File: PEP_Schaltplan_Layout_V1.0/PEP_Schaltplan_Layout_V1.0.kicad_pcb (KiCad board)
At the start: 2 copper layers, 202.5 x 119.7 mm, 140 parts, among them J1 Conn_01x02_Pin, J10 Conn_01x01_Pin, J11 Conn_01x02_Pin, J12 Conn_01x01_Pin, J2 Conn_01x01_Pin, J3 Conn_01x01_Pin, J4 Conn_01x01_Pin, J5 Conn_01x01_Pin, J6 Conn_01x01_Pin, J7 Conn_01x01_Pin, J8 Conn_01x01_Pin, J9 Conn_01x01_Pin, Q1 BC546, Q2 BC556, SW1 SW_DIP_x04, SW10 SW_DIP_x04, SW11 SW_DIP_x04, SW12 SW_DIP_x04, SW13 SW_DIP_x04, SW14 SW_DIP_x04, SW15 SW_DIP_x04, SW16 SW_DIP_x04, SW2 SW_DIP_x04, SW3 SW_DIP_x04, SW4 SW_DIP_x04, SW5 SW_DIP_x04, SW6 SW_DIP_x04, SW7 SW_DIP_x04, SW8 SW_DIP_x04, SW9 SW_DIP_x04, U1 AD822ANZ_new, U2 LM7805_TO220, U3 LM7905_TO220, U4 LT1819, U5 LT1819, U6 LT1819, U7 LT1819

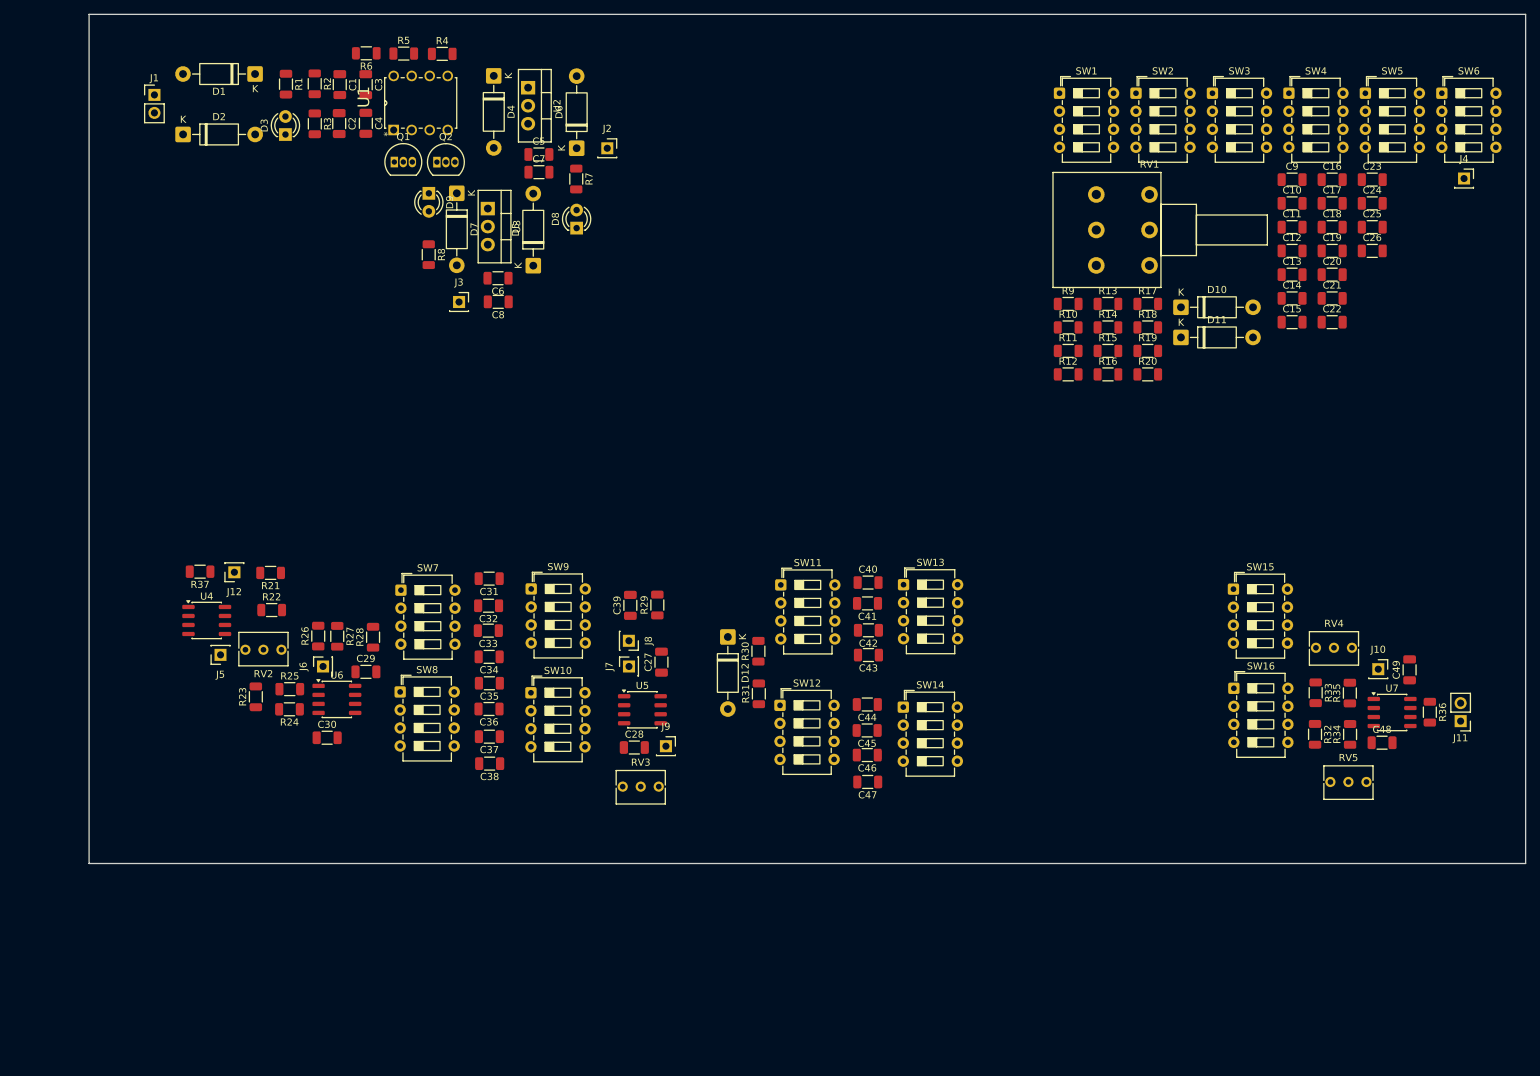
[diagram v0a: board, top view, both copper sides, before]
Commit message: Leiterplatten größe definiert und erstes Auto Routing
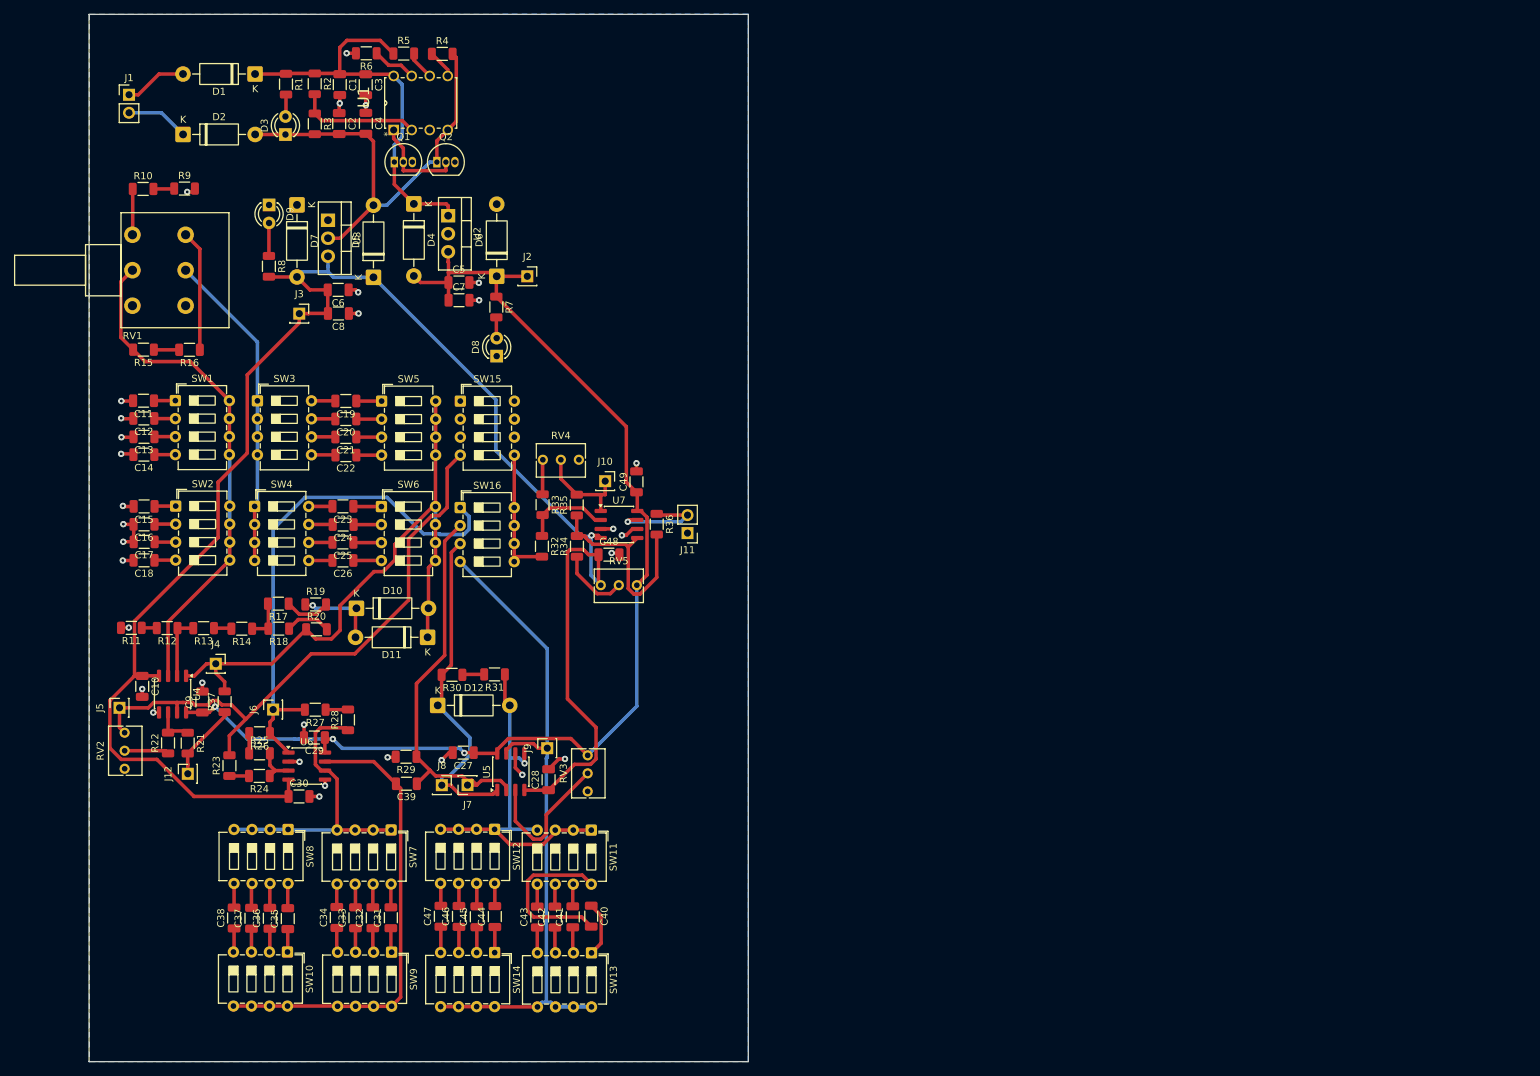
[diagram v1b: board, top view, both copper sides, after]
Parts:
- moved J4 188.8 mm to (64.1, 133.3)
- moved C10 175.8 mm to (53.7, 136.5), turned to -90 degrees
- moved C16 174.4 mm to (54.0, 113.6), turned to 180 degrees
- moved C17 174.1 mm to (54.0, 116.1), turned to 180 degrees
- moved C18 174.0 mm to (54.0, 118.7), turned to 180 degrees
- moved C9 170.4 mm to (62.2, 138.7), turned to 90 degrees
- moved C15 163.9 mm to (54.0, 111.1), turned to 180 degrees
- moved C11 163.8 mm to (53.9, 96.2), turned to 180 degrees
- moved C12 163.6 mm to (53.9, 98.7), turned to 180 degrees
- moved C13 163.5 mm to (54.0, 101.3), turned to 180 degrees
- moved C14 163.4 mm to (53.9, 103.8), turned to 180 degrees
- moved SW6 160.5 mm to (87.4, 111.1)
- moved SW4 157.0 mm to (69.6, 111.1)
- moved C23 152.2 mm to (82.0, 111.1), turned to 180 degrees
- moved C24 152.0 mm to (82.0, 113.7), turned to 180 degrees
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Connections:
- C10 pad 2: 0 -> GND
- C11 pad 2: 0 -> GND
- C12 pad 2: 0 -> GND
- C13 pad 2: 0 -> GND
- C14 pad 2: 0 -> GND
- C15 pad 2: 0 -> GND
- C16 pad 2: 0 -> GND
- C17 pad 2: 0 -> GND
- C18 pad 2: 0 -> GND
- C27 pad 2: 0 -> GND
- C28 pad 2: 0 -> GND
- C29 pad 2: 0 -> GND
- C30 pad 2: 0 -> GND
- C48 pad 2: 0 -> GND
- C49 pad 2: 0 -> GND
- C9 pad 2: 0 -> GND
- R11 pad 2: 0 -> GND
- R29 pad 2: 0 -> GND
- R9 pad 2: 0 -> GND
- RV3 pad 3: 0 -> GND
- U4 pad 5: 0 -> GND
- U5 pad 6: 0 -> GND
- U6 pad 2: 0 -> GND
- U6 pad 5: 0 -> GND
- U7 pad 3: 0 -> GND
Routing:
- net -5V: track 0.00 -> 247.3 mm, vias 0 -> 1
- net +5V: track 0.00 -> 168.8 mm, vias 0 -> 3
- net Sägezahn: track 0.00 -> 96.0 mm
- net Sinus_Wien: track 0.00 -> 87.7 mm
- net Sinus: track 0.00 -> 84.8 mm
- net Rechteck: track 0.00 -> 72.8 mm
- net Net-(U4A-+): track 0.00 -> 71.6 mm
- net Net-(C39-Pad2): track 0.00 -> 65.8 mm
- net -7.5V: track 0.00 -> 62.6 mm
- net +7.5V: track 0.00 -> 58.7 mm
- net GND: track 0.00 -> 55.5 mm, vias 0 -> 32
- net Net-(D12--): track 0.00 -> 55.1 mm, vias 0 -> 1
- net Dreieck: track 0.00 -> 54.5 mm
- net PWM: track 0.00 -> 48.2 mm
- net Net-(RV1-Pad5): track 0.00 -> 45.3 mm
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- added copper zone on B.Cu, net GND
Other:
- board size 202.5 x 119.7 mm -> 92.9 x 147.6 mm

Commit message: DRC Fehler Behoben
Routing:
- net -5V: track 247.3 -> 249.5 mm

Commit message: Geberdaten erstellt
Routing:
- net Net-(D12--): track 55.1 -> 56.2 mm
- net Net-(Q1-B): track 13.5 -> 14.6 mm
- net Net-(U5A-+): track 21.1 -> 22.1 mm
- net Dreieck: track 54.5 -> 53.6 mm

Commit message: Anpassung
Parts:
- R25: value 190k -> 200k
- R9: value 500 -> 510
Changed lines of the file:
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@@
 			)
 		)
-		(property "Value" "500"
+		(property "Value" "510"
 			(at 0 1.83 0)
 			(layer "F.Fab")
@@
 			)
 		)
-		(property "Value" "190k"
+		(property "Value" "200k"
 			(at 0 1.83 0)
 			(layer "F.Fab")
@@
 			)
 		)
-		(property "Description" ""
+		(property "Description" "Eigentlich 190k"
 			(at 0 0 0)
 			(layer "F.Fab")
